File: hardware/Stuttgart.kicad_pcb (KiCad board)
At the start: 2 copper layers, 85.5 x 63.5 mm, 21 parts, among them IC1 NCV1117ST33T3G, J1 USB_C_Receptacle_USB2.0_16P, U1 RP2354A

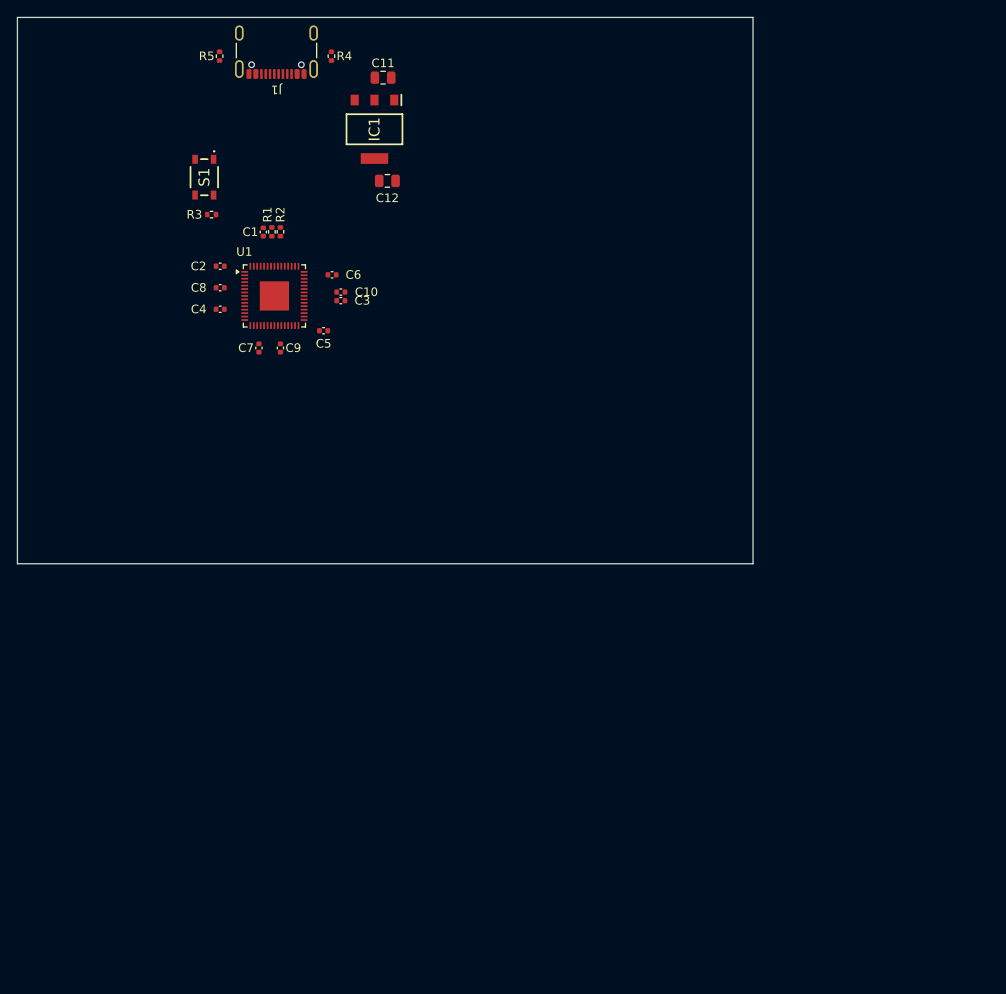
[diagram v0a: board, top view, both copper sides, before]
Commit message: Most RP components on board. Core regulator wired up
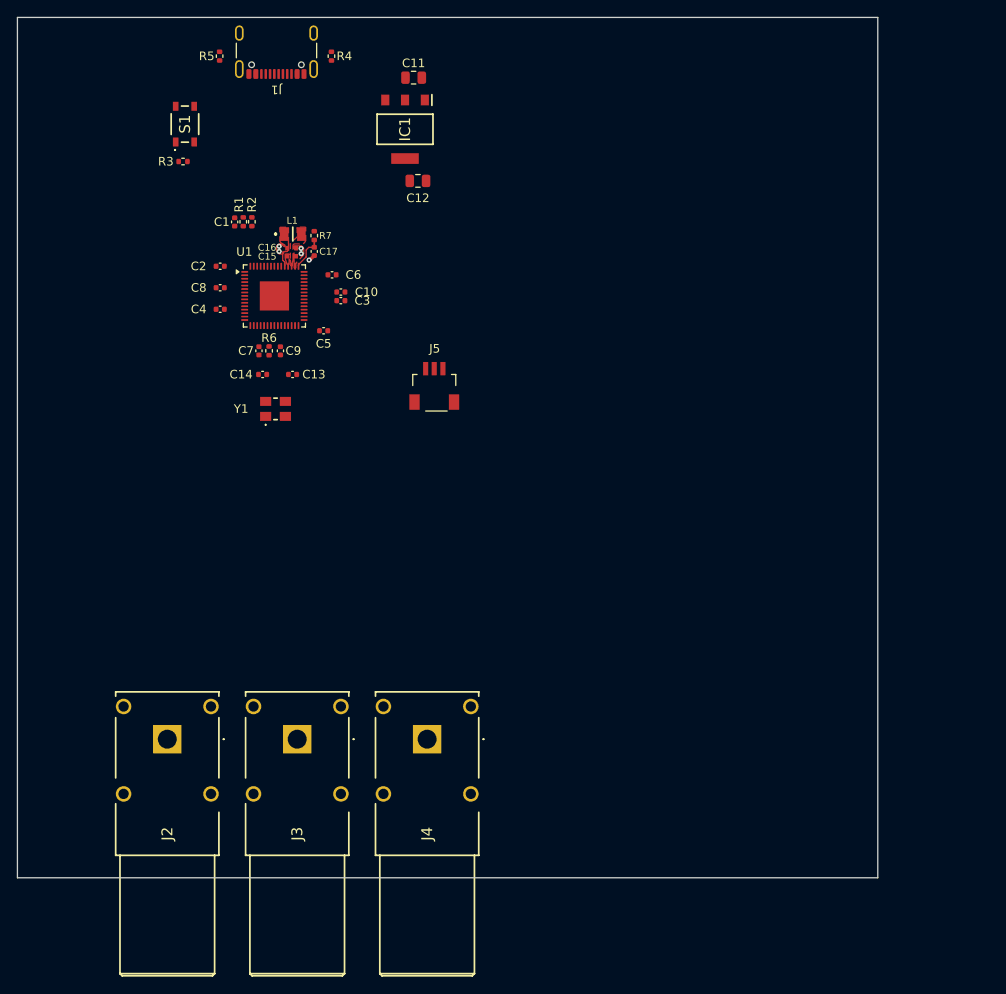
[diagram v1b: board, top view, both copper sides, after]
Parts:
- added C13: 15p, Capacitor_SMD:C_0402_1005Metric, F.Cu at (135.0, 97.0)
- added C14: 15p, Capacitor_SMD:C_0402_1005Metric, F.Cu at (131.5, 97.0)
- added C15: 4.7u, Stuttgart:C_0402_1005Metric_small_pads, F.Cu at (134.9, 83.3)
- added C16: 4.7u, Stuttgart:C_0402_1005Metric_small_pads, F.Cu at (134.9, 82.3)
- added C17: 4.7u, Capacitor_SMD:C_0402_1005Metric, F.Cu at (137.5, 82.7)
- added J2: FCR7350, Stuttgart:FCR7350G, F.Cu at (120.4, 139.4)
- added J3: FCR7350, Stuttgart:FCR7350G, F.Cu at (135.5, 139.4)
- added J4: FCR7350, Stuttgart:FCR7350G, F.Cu at (150.6, 139.4)
- added J5: SM03B-SRSS-TB_LF__SN_, Stuttgart:SM03BSRSSTBLFSN, F.Cu at (151.4, 98.8)
- added L1: AOTA-B201610S3R3-101-T, Stuttgart:AOTAB201610S3R3101T, F.Cu at (135.0, 80.7)
- added R6: 1k, Resistor_SMD:R_0402_1005Metric, F.Cu at (132.2, 94.2)
- added R7: 33, Resistor_SMD:R_0402_1005Metric, F.Cu at (137.5, 80.9)
- added Y1: ABM8-272-T3, Stuttgart:ABM8272T3, F.Cu at (133.0, 101.0)
- moved R3 7.01 mm to (122.2, 72.2)
- moved S1 6.57 mm to (122.5, 67.9), turned to 90 degrees
- moved C11 3.55 mm to (149.1, 62.5)
- moved C12 3.55 mm to (149.6, 74.5)
- moved IC1 3.55 mm to (148.1, 68.5)
- moved C1 3.52 mm to (128.2, 79.3)
- moved R1 3.52 mm to (129.2, 79.2)
- moved R2 3.52 mm to (130.2, 79.2)
- moved C7 0.33 mm to (131.1, 94.2)
- moved C9 0.33 mm to (133.6, 94.2)
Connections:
- R3 pad 1: Net-(S1-NO_2) -> /RP2354A/BOOT_NO
- S1 pad 1: unconnected-(S1-NO_1-Pad1) -> /RP2354A/BOOT_NO
- S1 pad 2: Net-(S1-NO_2) -> /RP2354A/BOOT_NO
- S1 pad 4: unconnected-(S1-COM_2-Pad4) -> GND
- U1 pad 21: unconnected-(U1-XIN-Pad21) -> /RP2354A/XIN
- U1 pad 22: unconnected-(U1-XOUT-Pad22) -> /RP2354A/XOUT
- U1 pad 24: unconnected-(U1-SWCLK-Pad24) -> /RP2354A/SWCLK
- U1 pad 25: unconnected-(U1-SWDIO-Pad25) -> /RP2354A/SWD
- U1 pad 26: unconnected-(U1-RUN-Pad26) -> +3V3
- U1 pad 46: unconnected-(U1-VREG_AVDD-Pad46) -> /RP2354A/VREG_AVDD
- U1 pad 47: unconnected-(U1-VREG_PGND-Pad47) -> GND
- U1 pad 48: unconnected-(U1-VREG_LX-Pad48) -> /RP2354A/VREG_LX
- U1 pad 49: unconnected-(U1-VREG_VIN-Pad49) -> +3V3
- U1 pad 50: unconnected-(U1-VREG_FB-Pad50) -> +1V1
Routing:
- net /RP2354A/VREG_AVDD: track 0.00 -> 4.34 mm
- net +1V1: track 0.00 -> 1.78 mm, vias 0 -> 2
- net GND: track 0.00 -> 0.82 mm, vias 0 -> 3
- added copper zone on F.Cu, net +1V1
- added copper zone on F.Cu, net +3V3
- added copper zone on F.Cu, net /RP2354A/VREG_LX
- added copper zone on F.Cu, net GND
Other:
- board size 85.5 x 63.5 mm -> 100 x 100 mm

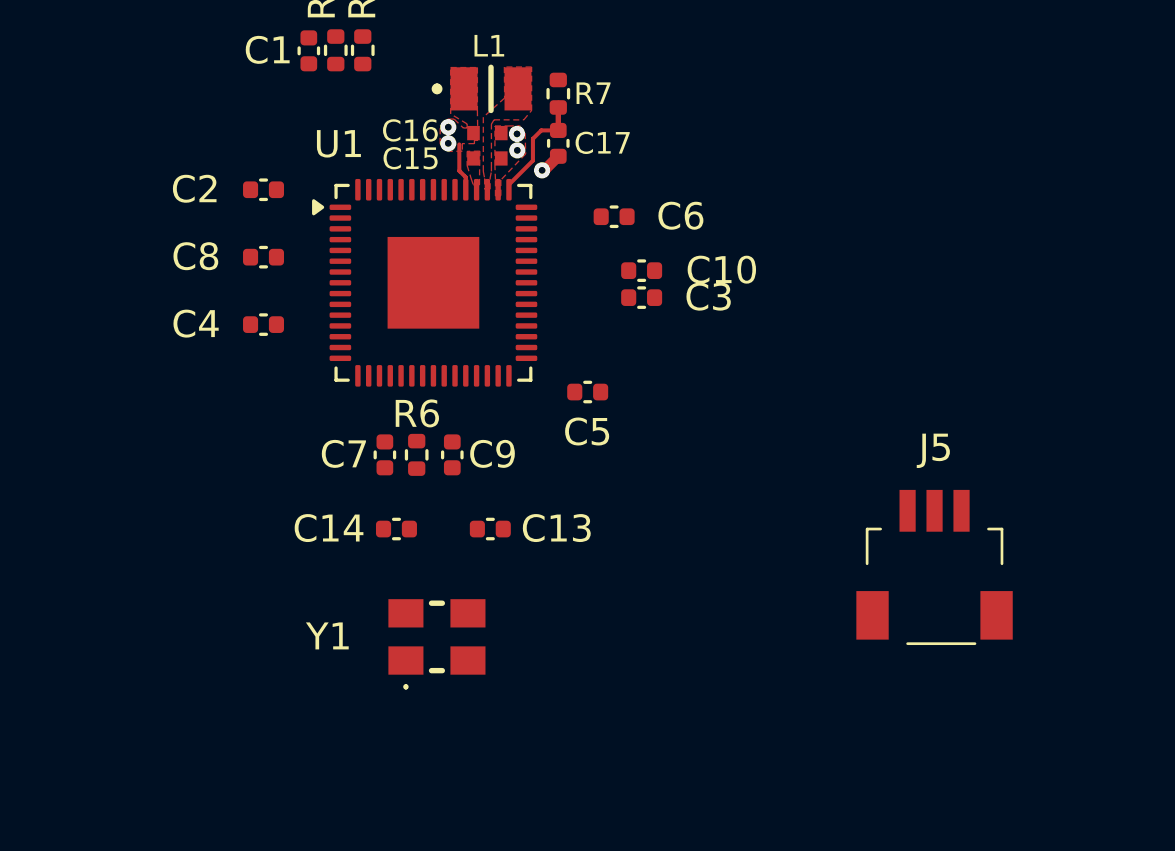
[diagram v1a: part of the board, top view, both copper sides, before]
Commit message: Wired in RP Crystal
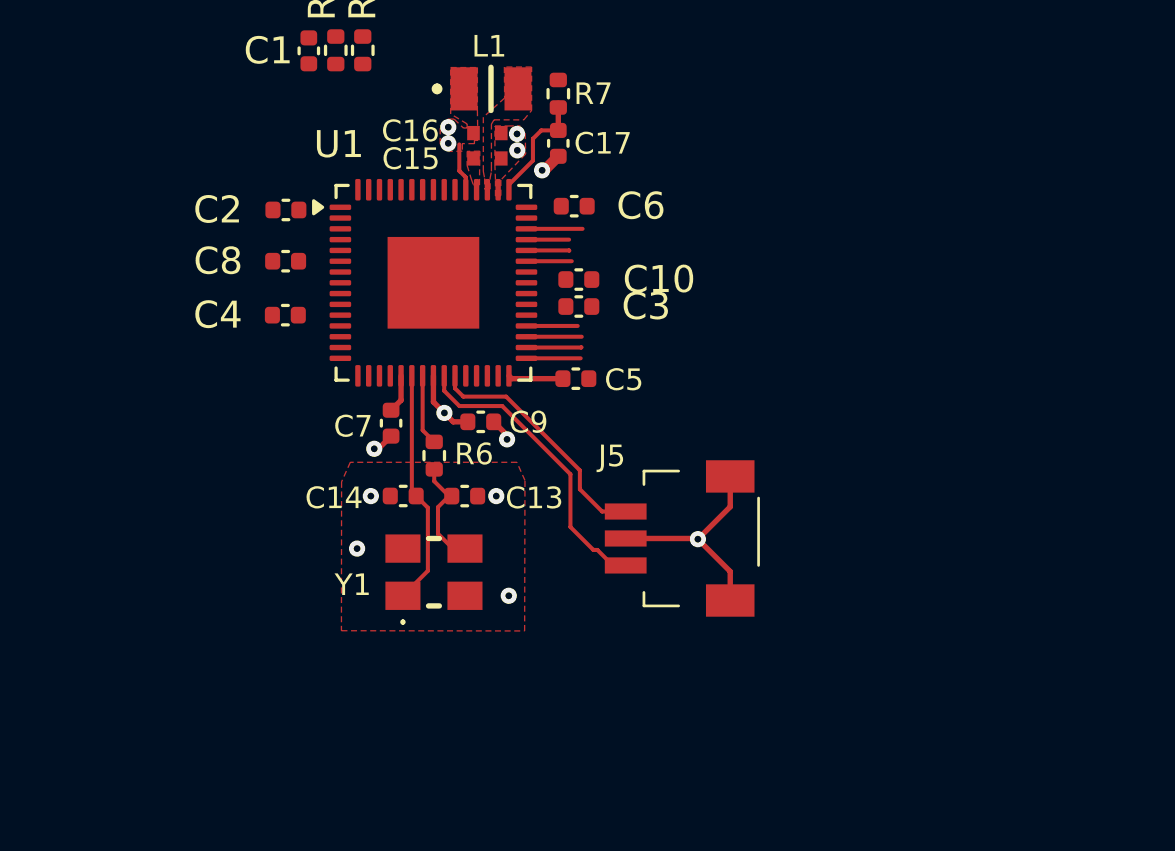
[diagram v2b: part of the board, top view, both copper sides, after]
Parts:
- moved J5 9.10 mm to (142.5, 97.3), turned to 90 degrees
- moved Y1 2.40 mm to (132.9, 98.6)
- moved C10 2.35 mm to (138.3, 87.8)
- moved C3 2.35 mm to (138.3, 88.8)
- moved C9 1.62 mm to (134.6, 93.0), turned to 0 degrees
- moved C13 1.55 mm to (134.0, 95.8)
- moved C6 1.53 mm to (138.1, 85.0)
- moved C14 1.25 mm to (131.8, 95.8)
- moved C7 1.20 mm to (131.3, 93.1)
- moved C2 1.12 mm to (127.4, 85.2)
- moved C4 0.88 mm to (127.4, 89.1)
- moved C8 0.83 mm to (127.4, 87.1)
- moved C5 0.66 mm to (138.2, 91.4)
- moved R6 0.65 mm to (132.9, 94.3)
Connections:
- U1 pad 31: unconnected-(U1-GPIO19-Pad31) -> /RP2354A/SPI0_TX
- U1 pad 32: unconnected-(U1-GPIO20-Pad32) -> /RP2354A/SPI0_RX
- U1 pad 33: unconnected-(U1-GPIO21-Pad33) -> /RP2354A/CAN_STBY
- U1 pad 34: unconnected-(U1-GPIO22-Pad34) -> /RP2354A/SPI0_SCK
- U1 pad 40: unconnected-(U1-GPIO26/ADC0-Pad40) -> /RP2354A/SPI1_SCK
- U1 pad 41: unconnected-(U1-GPIO27/ADC1-Pad41) -> /RP2354A/SPI1_TX
- U1 pad 42: unconnected-(U1-GPIO28/ADC2-Pad42) -> /RP2354A/SPI1_RX
- U1 pad 43: unconnected-(U1-GPIO29/ADC3-Pad43) -> /RP2354A/CAN_INTERRUPT
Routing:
- net /RP2354A/SWCLK: track 0.00 -> 11.1 mm
- net GND: track 0.82 -> 10.8 mm, vias 3 -> 10
- net /RP2354A/SWD: track 0.00 -> 9.09 mm
- net /RP2354A/XIN: track 0.00 -> 8.78 mm
- net Net-(Y1-CRYSTAL_2): track 0.00 -> 4.11 mm
- net +3V3: track 0.00 -> 3.69 mm
- net /RP2354A/XOUT: track 0.00 -> 2.63 mm
- net +1V1: track 1.78 -> 4.33 mm, vias 2 -> 3
- net /RP2354A/CAN_INTERRUPT: track 0.00 -> 2.08 mm
- net /RP2354A/CAN_STBY: track 0.00 -> 2.05 mm
- net /RP2354A/SPI0_RX: track 0.00 -> 2.04 mm
- net /RP2354A/SPI0_TX: track 0.00 -> 2.01 mm
- net /RP2354A/SPI0_SCK: track 0.00 -> 1.90 mm
- net /RP2354A/SPI1_SCK: track 0.00 -> 1.68 mm
- net /RP2354A/SPI1_TX: track 0.00 -> 1.59 mm
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
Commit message: Further RP development - Kicad keeps crashing
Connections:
- U1 pad 61: unconnected-(U1-GND-Pad61) -> GND
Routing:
- net +1V1: track 4.33 -> 14.5 mm, vias 3 -> 8
- net GND: track 10.8 -> 15.3 mm, vias 10 -> 12
- added copper zone on B.Cu, net GND

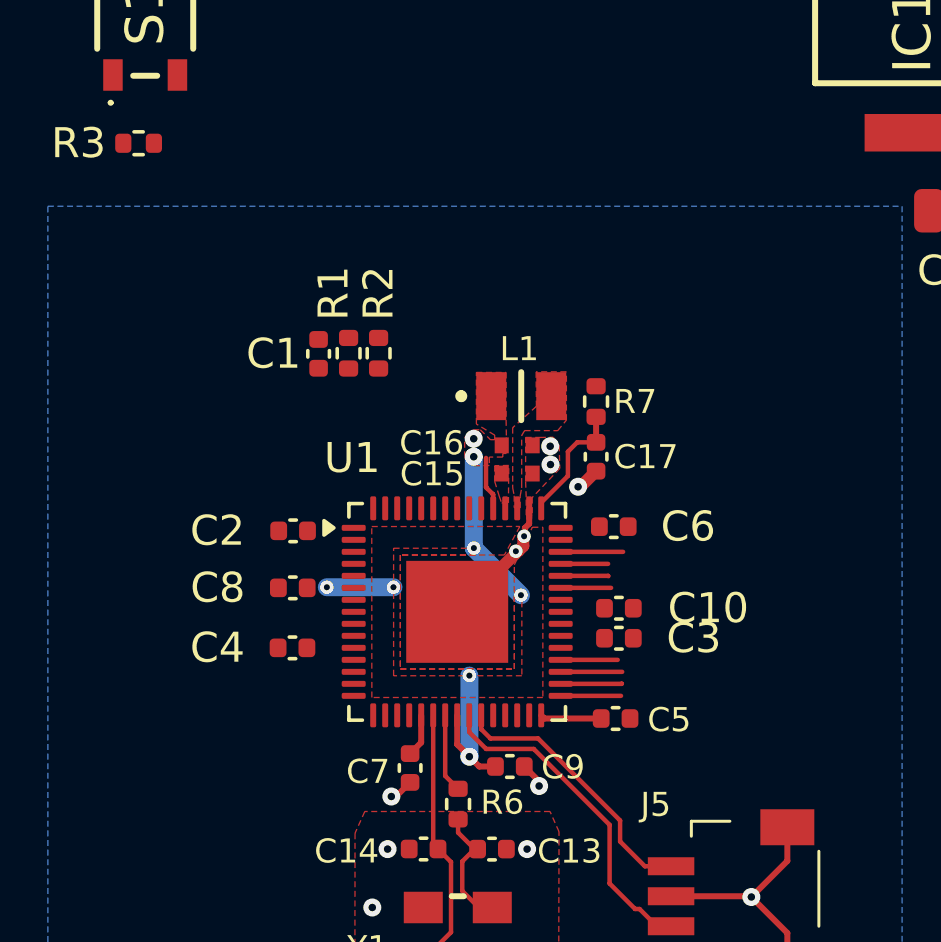
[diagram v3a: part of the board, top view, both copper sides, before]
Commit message: Core RP pad work complete
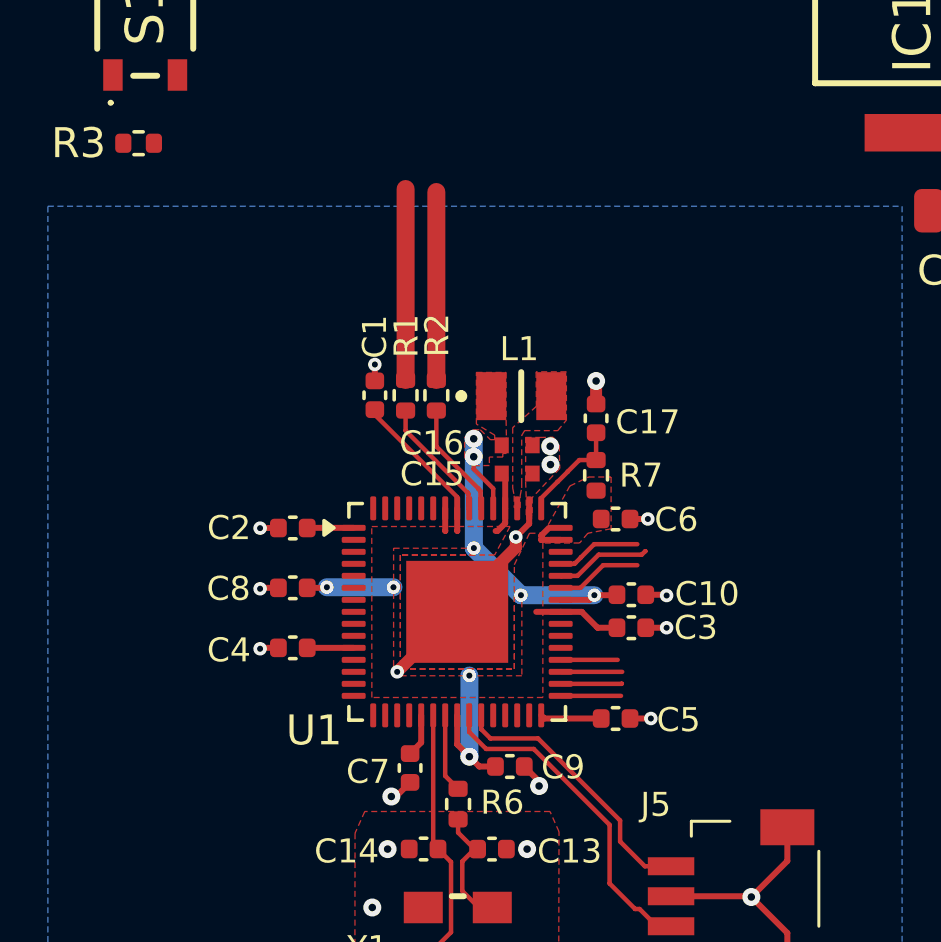
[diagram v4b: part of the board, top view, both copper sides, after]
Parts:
- moved R7 2.46 mm to (137.5, 83.3), turned to 90 degrees
- moved R2 2.38 mm to (132.2, 80.7)
- moved R1 2.36 mm to (131.2, 80.7)
- moved C1 2.33 mm to (130.1, 80.7)
- moved C17 1.28 mm to (137.5, 81.4), turned to 90 degrees
- moved C10 0.61 mm to (138.7, 87.3)
- moved C3 0.54 mm to (138.7, 88.4)
- moved C6 0.26 mm to (138.2, 84.8)
- moved C2 0.10 mm to (127.4, 85.1)
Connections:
- U1 pad 43: /RP2354A/CAN_INTERRUPT -> unconnected-(U1-GPIO29/ADC3-Pad43)
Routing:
- net +3V3: track 3.69 -> 19.0 mm
- net GND: track 15.3 -> 23.1 mm, vias 12 -> 20
- net USB_D+: track 0.00 -> 6.36 mm
- net USB_D-: track 0.00 -> 6.27 mm
- net +1V1: track 14.5 -> 20.4 mm, vias 8 -> 9
- net Net-(U1-USB_DP): track 0.00 -> 4.15 mm
- net Net-(U1-USB_DM): track 0.00 -> 3.89 mm
- net /RP2354A/CAN_INTERRUPT: track 2.08 -> 0.00 mm
- net /RP2354A/SPI1_TX: track 1.59 -> 3.21 mm
- net /RP2354A/SPI1_RX: track 1.58 -> 2.83 mm
- net /RP2354A/SPI1_SCK: track 1.68 -> 2.87 mm
- net /RP2354A/VREG_AVDD: track 4.34 -> 3.80 mm

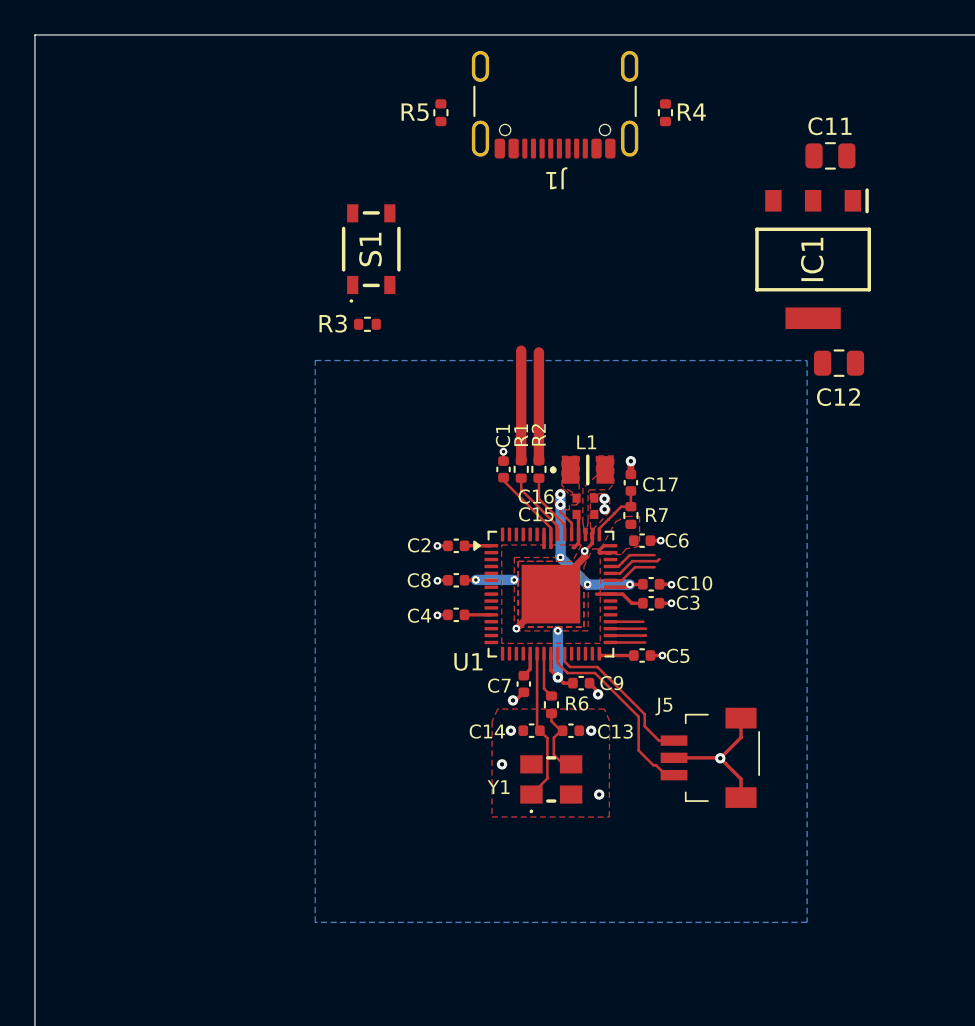
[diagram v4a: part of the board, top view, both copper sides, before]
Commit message: Boot select button added
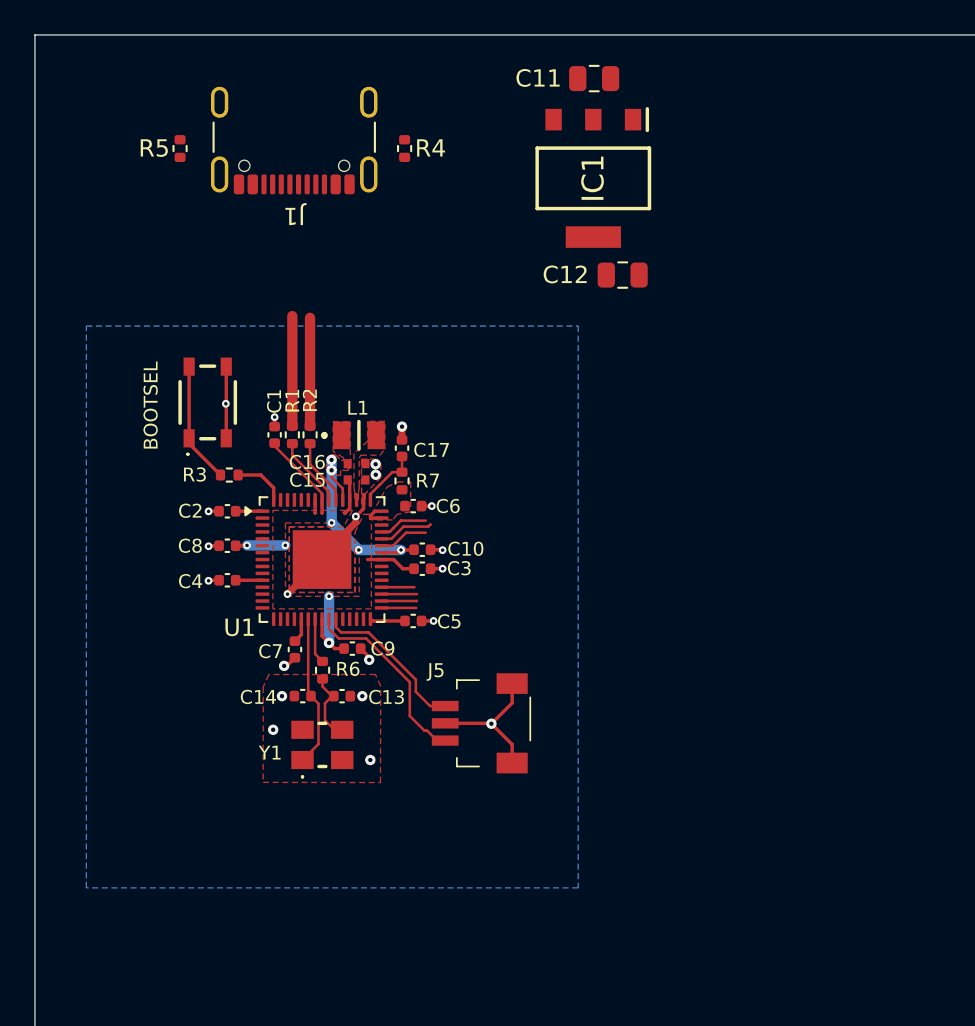
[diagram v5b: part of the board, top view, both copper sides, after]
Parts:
- moved J1 15.2 mm to (118.0, 60.5)
- moved R4 15.2 mm to (124.4, 62.1)
- moved R5 15.2 mm to (111.4, 62.1)
- moved C11 14.4 mm to (135.4, 58.0)
- moved IC1 13.6 mm to (135.3, 63.8)
- moved C12 13.5 mm to (137.0, 69.4)
- moved C10 13.4 mm to (125.4, 85.3)
- moved C3 13.4 mm to (125.4, 86.4)
- moved C7 13.4 mm to (118.0, 91.1)
- moved R2 13.4 mm to (118.9, 78.7)
- moved C1 13.4 mm to (116.9, 78.7)
- moved C13 13.4 mm to (120.8, 93.8)
- moved C14 13.4 mm to (118.5, 93.8)
- moved C15 13.4 mm to (121.6, 81.3)
- moved C16 13.4 mm to (121.6, 80.3)
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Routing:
- net /RP2354A/BOOT_NO: track 0.00 -> 7.03 mm
- net GND: track 23.1 -> 27.3 mm, vias 20 -> 21
- net /RP2354A/USB_BOOT: track 0.00 -> 3.07 mm
